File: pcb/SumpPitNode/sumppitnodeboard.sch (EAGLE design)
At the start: 21 parts

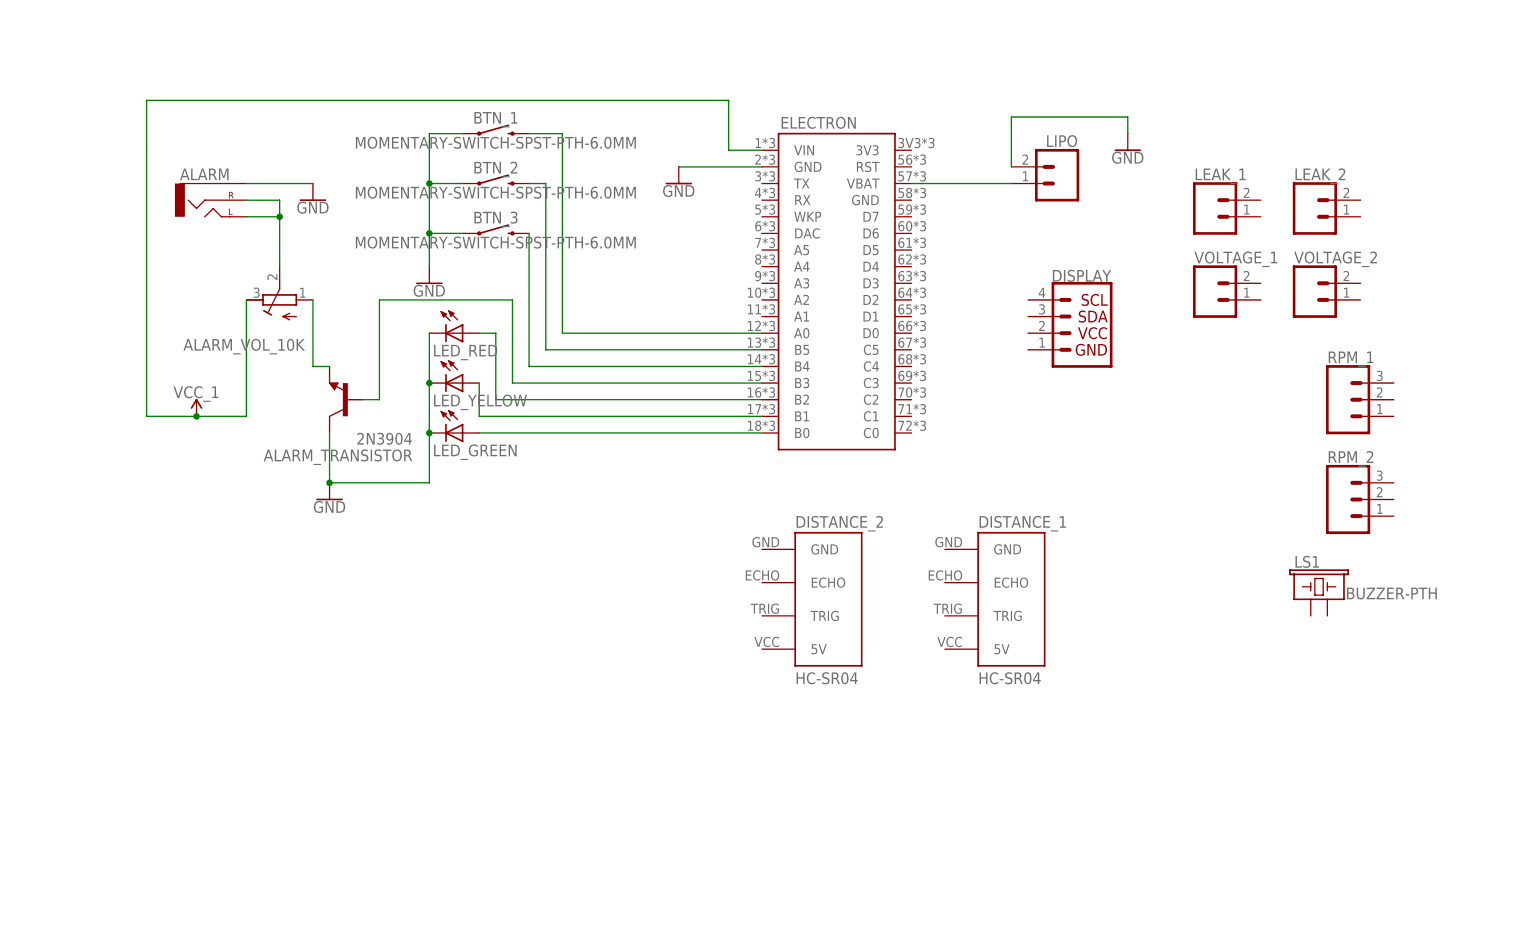
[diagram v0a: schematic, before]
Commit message: Connect more wires. distance to interrupt pins. i2c display 5v voltage regulator for distance sensor. add resistors for leds.
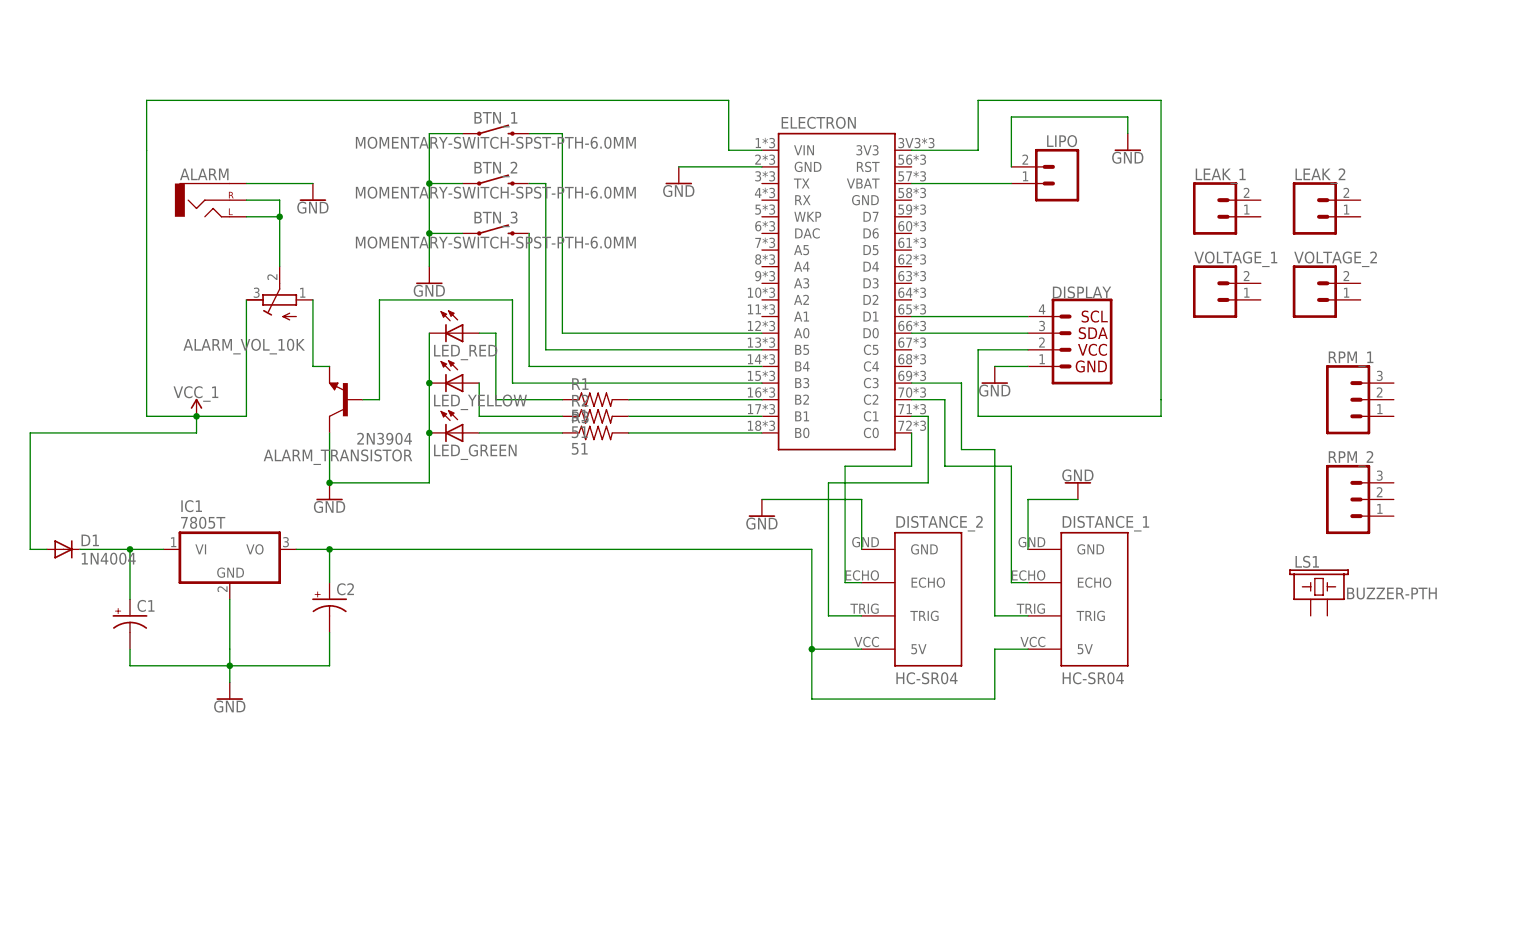
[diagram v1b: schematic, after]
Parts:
- added C1, C2: (no value), rcl:CPOL-USE1.8-4
- added D1: 1N4004, diode:1N4004
- added IC1: 7805T, linear:7805T
- added R1, R2, R3: 51, resistor:R-US_0204/5
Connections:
- new net N$11: DISPLAY.3, ELECTRON.D0
- new net N$12: DISPLAY.4, ELECTRON.D1
- new net N$13: DISTANCE_1.ECHO, ELECTRON.C2
- new net N$14: DISPLAY.2, ELECTRON.3V3
- new net N$15: DISTANCE_2.ECHO, ELECTRON.C0
- new net N$16: DISTANCE_2.TRIG, ELECTRON.C1
- new net N$17: DISTANCE_1.TRIG, ELECTRON.C3
- new net N$18: C1.+, D1.C, IC1.VI
- new net N$19: ELECTRON.B2, R1.2
- new net N$20: LED_YELLOW.A, R2.1
- new net N$21: LED_GREEN.A, R3.1
- new net N$23: C2.+, DISTANCE_1.5V, DISTANCE_2.5V, IC1.VO
- net B$11: now also D1.A
- net GND: now also C1.-, C2.-, DISPLAY.1, DISTANCE_1.GND, DISTANCE_2.GND, IC1.GND
- net N$4: now also R1.1; no longer ELECTRON.B2
- net N$5: now also R2.2; no longer LED_YELLOW.A
- net N$6: now also R3.2; no longer LED_GREEN.A
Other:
- moved on the sheet: DISPLAY, DISTANCE_1, DISTANCE_2

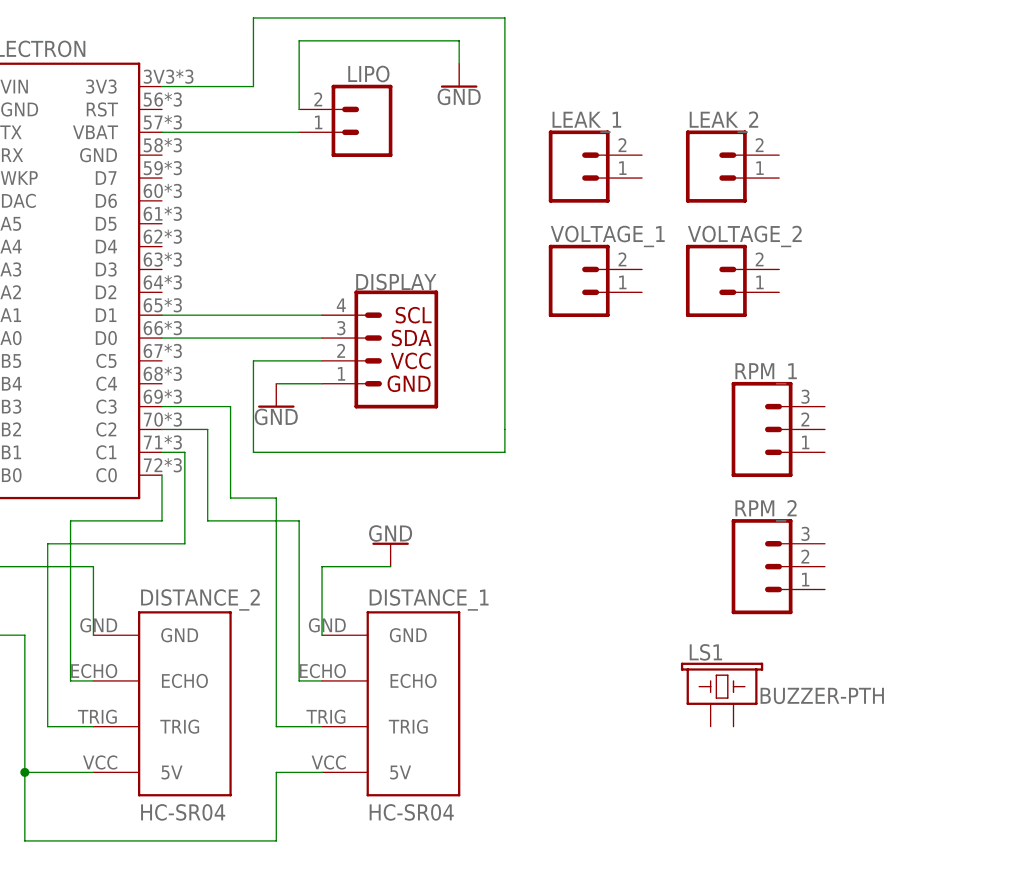
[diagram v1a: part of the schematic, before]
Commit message: Connect buzzer.
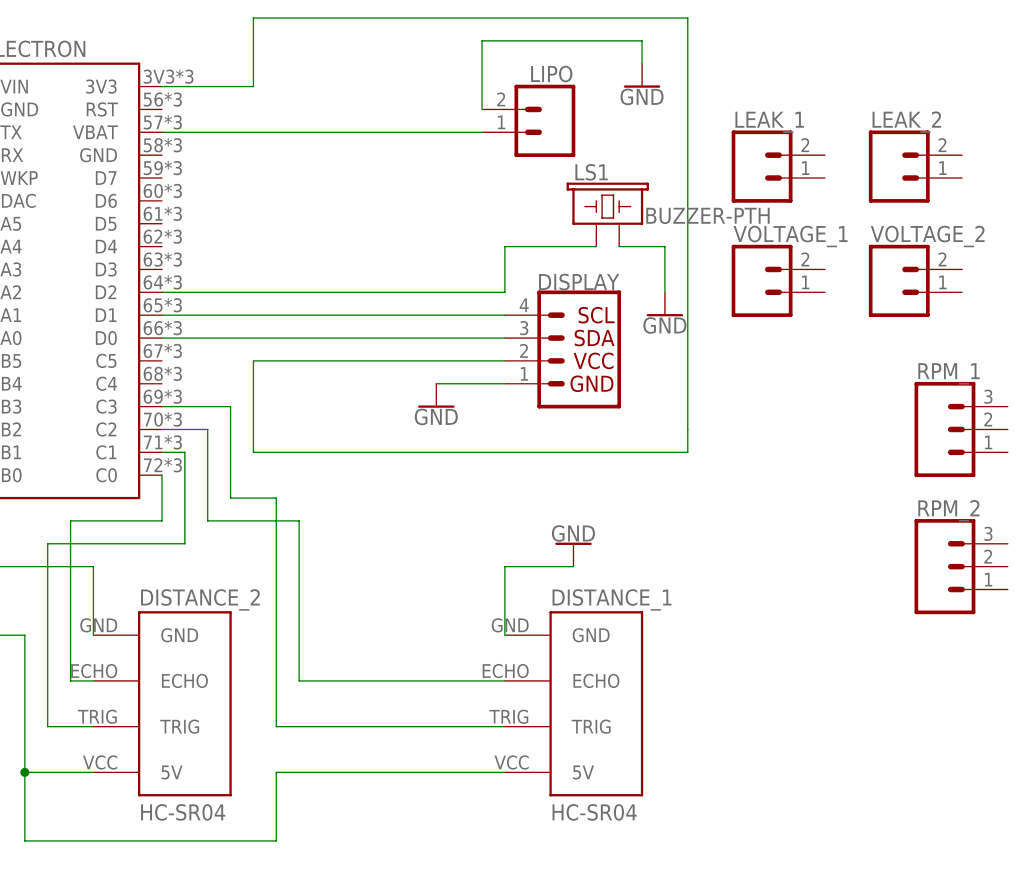
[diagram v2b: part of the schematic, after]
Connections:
- new net N$22: ELECTRON.D2, LS1.1
- net GND: now also LS1.2
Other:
- moved on the sheet: DISPLAY, DISTANCE_1, LEAK_1, LEAK_2, LIPO, LS1, RPM_1, RPM_2, VOLTAGE_1, VOLTAGE_2
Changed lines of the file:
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@@
 <part name="R2" library="resistor" library_urn="urn:adsk.eagle:library:348" deviceset="R-US_" device="0204/5" package3d_urn="urn:adsk.eagle:package:25955/1" value="51"/>
 <part name="R3" library="resistor" library_urn="urn:adsk.eagle:library:348" deviceset="R-US_" device="0204/5" package3d_urn="urn:adsk.eagle:package:25955/1" value="51"/>
+<part name="GND10" library="SparkFun-PowerSymbols" library_urn="urn:adsk.eagle:library:530" deviceset="GND" device=""/>
 </parts>
 <sheets>
@@
 <instances>
 <instance part="ELECTRON" gate="G$1" x="-35.56" y="60.96"/>
-<instance part="DISPLAY" gate="G$1" x="2.54" y="50.8" rot="MR0"/>
-<instance part="DISTANCE_1" gate="J_ULTRASONIC" x="7.62" y="12.7"/>
+<instance part="DISPLAY" gate="G$1" x="22.86" y="50.8" rot="MR0"/>
+<instance part="DISTANCE_1" gate="J_ULTRASONIC" x="27.94" y="12.7"/>
 <instance part="DISTANCE_2" gate="J_ULTRASONIC" x="-17.78" y="12.7"/>
-<instance part="LEAK_1" gate="G$1" x="22.86" y="71.12"/>
-<instance part="LEAK_2" gate="G$1" x="38.1" y="71.12"/>
-<instance part="VOLTAGE_1" gate="G$1" x="22.86" y="58.42"/>
-<instance part="VOLTAGE_2" gate="G$1" x="38.1" y="58.42"/>
-<instance part="RPM_1" gate="J$1" x="43.18" y="43.18"/>
-<instance part="RPM_2" gate="J$1" x="43.18" y="27.94"/>
+<instance part="LEAK_1" gate="G$1" x="43.18" y="71.12"/>
+<instance part="LEAK_2" gate="G$1" x="58.42" y="71.12"/>
+<instance part="VOLTAGE_1" gate="G$1" x="43.18" y="58.42"/>
+<instance part="VOLTAGE_2" gate="G$1" x="58.42" y="58.42"/>
+<instance part="RPM_1" gate="J$1" x="63.5" y="43.18"/>
+<instance part="RPM_2" gate="J$1" x="63.5" y="27.94"/>
 <instance part="LED_YELLOW" gate="G$1" x="-91.44" y="45.72" rot="R270"/>
 <instance part="LED_GREEN" gate="G$1" x="-91.44" y="38.1" rot="R270"/>
 <instance part="LED_RED" gate="G$1" x="-91.44" y="53.34" rot="R270"/>
-<instance part="LS1" gate="G$1" x="38.1" y="12.7"/>
+<instance part="LS1" gate="G$1" x="25.4" y="66.04"/>
 <instance part="ALARM" gate="G$1" x="-129.54" y="73.66"/>
 <instance part="BTN_1" gate="G$1" x="-86.36" y="83.82"/>
 <instance part="BTN_2" gate="G$1" x="-86.36" y="76.2"/>
 <instance part="BTN_3" gate="G$1" x="-86.36" y="68.58"/>
-<instance part="LIPO" gate="G$1" x="0" y="76.2" rot="MR0"/>
+<instance part="LIPO" gate="G$1" x="20.32" y="76.2" rot="MR0"/>
 <instance part="ALARM_TRANSISTOR" gate="G1" x="-109.22" y="43.18" rot="R180"/>
 <instance part="ALARM_VOL_10K" gate="G$1" x="-119.38" y="58.42" rot="R90"/>
@@
 <instance part="GND2" gate="1" x="-111.76" y="27.94"/>
 <instance part="GND3" gate="1" x="-58.42" y="76.2"/>
-<instance part="GND4" gate="1" x="10.16" y="81.28"/>
+<instance part="GND4" gate="1" x="30.48" y="81.28"/>
 <instance part="GND5" gate="1" x="-96.52" y="60.96"/>
-<instance part="GND6" gate="1" x="-10.16" y="45.72"/>
+<instance part="GND6" gate="1" x="7.62" y="45.72"/>
 <instance part="IC1" gate="A1" x="-127" y="20.32"/>
 <instance part="D1" gate="1" x="-152.4" y="20.32"/>
@@
 <instance part="C2" gate="G$1" x="-111.76" y="12.7"/>
 <instance part="GND7" gate="1" x="-127" y="-2.54"/>
-<instance part="GND8" gate="1" x="2.54" y="30.48" rot="R180"/>
+<instance part="GND8" gate="1" x="22.86" y="30.48" rot="R180"/>
 <instance part="GND9" gate="1" x="-45.72" y="25.4"/>
 <instance part="R1" gate="G$1" x="-71.12" y="43.18"/>
 <instance part="R2" gate="G$1" x="-71.12" y="40.64"/>
 <instance part="R3" gate="G$1" x="-71.12" y="38.1"/>
+<instance part="GND10" gate="1" x="33.02" y="55.88"/>
 </instances>
 <busses>
@@
 <segment>
 <pinref part="LIPO" gate="G$1" pin="2"/>
-<wire x1="-7.62" y1="78.74" x2="-7.62" y2="86.36" width="0.1524" layer="91"/>
-<wire x1="-7.62" y1="86.36" x2="10.16" y2="86.36" width="0.1524" layer="91"/>
+<wire x1="12.7" y1="78.74" x2="12.7" y2="86.36" width="0.1524" layer="91"/>
+<wire x1="12.7" y1="86.36" x2="30.48" y2="86.36" width="0.1524" layer="91"/>
 <pinref part="GND4" gate="1" pin="GND"/>
-<wire x1="10.16" y1="86.36" x2="10.16" y2="83.82" width="0.1524" layer="91"/>
+<wire x1="30.48" y1="86.36" x2="30.48" y2="83.82" width="0.1524" layer="91"/>
 </segment>
 <segment>
@@
 <pinref part="GND6" gate="1" pin="GND"/>
 <pinref part="DISPLAY" gate="G$1" pin="1"/>
-<wire x1="-10.16" y1="48.26" x2="-5.08" y2="48.26" width="0.1524" layer="91"/>
+<wire x1="7.62" y1="48.26" x2="15.24" y2="48.26" width="0.1524" layer="91"/>
 </segment>
 <segment>
@@
 <segment>
 <pinref part="DISTANCE_1" gate="J_ULTRASONIC" pin="GND"/>
-<wire x1="-5.08" y1="20.32" x2="-5.08" y2="27.94" width="0.1524" layer="91"/>
+<wire x1="15.24" y1="20.32" x2="15.24" y2="27.94" width="0.1524" layer="91"/>
 <pinref part="GND8" gate="1" pin="GND"/>
-<wire x1="-5.08" y1="27.94" x2="2.54" y2="27.94" width="0.1524" layer="91"/>
+<wire x1="15.24" y1="27.94" x2="22.86" y2="27.94" width="0.1524" layer="91"/>
+</segment>
+<segment>
+<pinref part="LS1" gate="G$1" pin="2"/>
+<wire x1="27.94" y1="63.5" x2="33.02" y2="63.5" width="0.1524" layer="91"/>
+<pinref part="GND10" gate="1" pin="GND"/>
+<wire x1="33.02" y1="63.5" x2="33.02" y2="58.42" width="0.1524" layer="91"/>
 </segment>
 </net>
@@
 <pinref part="LIPO" gate="G$1" pin="1"/>
 <pinref part="ELECTRON" gate="G$1" pin="VBAT"/>
-<wire x1="-7.62" y1="76.2" x2="-22.86" y2="76.2" width="0.1524" layer="91"/>
+<wire x1="12.7" y1="76.2" x2="-22.86" y2="76.2" width="0.1524" layer="91"/>
 </segment>
 </net>
@@
 <pinref part="ELECTRON" gate="G$1" pin="D0"/>
 <pinref part="DISPLAY" gate="G$1" pin="3"/>
-<wire x1="-22.86" y1="53.34" x2="-5.08" y2="53.34" width="0.1524" layer="91"/>
+<wire x1="-22.86" y1="53.34" x2="15.24" y2="53.34" width="0.1524" layer="91"/>
 </segment>
 </net>
@@
 <pinref part="DISPLAY" gate="G$1" pin="4"/>
 <pinref part="ELECTRON" gate="G$1" pin="D1"/>
-<wire x1="-5.08" y1="55.88" x2="-22.86" y2="55.88" width="0.1524" layer="91"/>
+<wire x1="15.24" y1="55.88" x2="-22.86" y2="55.88" width="0.1524" layer="91"/>
 </segment>
 </net>
@@
 <segment>
 <pinref part="DISPLAY" gate="G$1" pin="2"/>
-<wire x1="-12.7" y1="50.8" x2="-5.08" y2="50.8" width="0.1524" layer="91"/>
+<wire x1="-12.7" y1="50.8" x2="15.24" y2="50.8" width="0.1524" layer="91"/>
 <wire x1="-12.7" y1="50.8" x2="-12.7" y2="40.64" width="0.1524" layer="91"/>
-<wire x1="-12.7" y1="40.64" x2="15.24" y2="40.64" width="0.1524" layer="91"/>
-<wire x1="15.24" y1="40.64" x2="15.24" y2="43.18" width="0.1524" layer="91"/>
-<wire x1="15.24" y1="43.18" x2="15.24" y2="88.9" width="0.1524" layer="91"/>
-<wire x1="15.24" y1="88.9" x2="-12.7" y2="88.9" width="0.1524" layer="91"/>
+<wire x1="-12.7" y1="40.64" x2="35.56" y2="40.64" width="0.1524" layer="91"/>
+<wire x1="35.56" y1="40.64" x2="35.56" y2="43.18" width="0.1524" layer="91"/>
+<wire x1="35.56" y1="43.18" x2="35.56" y2="88.9" width="0.1524" layer="91"/>
+<wire x1="35.56" y1="88.9" x2="-12.7" y2="88.9" width="0.1524" layer="91"/>
 <pinref part="ELECTRON" gate="G$1" pin="3V3"/>
 <wire x1="-22.86" y1="81.28" x2="-12.7" y2="81.28" width="0.1524" layer="91"/>
@@
 <segment>
 <pinref part="DISTANCE_1" gate="J_ULTRASONIC" pin="ECHO"/>
-<wire x1="-5.08" y1="15.24" x2="-7.62" y2="15.24" width="0.1524" layer="91"/>
+<wire x1="15.24" y1="15.24" x2="-7.62" y2="15.24" width="0.1524" layer="91"/>
 <wire x1="-7.62" y1="15.24" x2="-7.62" y2="33.02" width="0.1524" layer="91"/>
 <wire x1="-7.62" y1="33.02" x2="-17.78" y2="33.02" width="0.1524" layer="91"/>
@@
 <wire x1="-10.16" y1="35.56" x2="-10.16" y2="10.16" width="0.1524" layer="91"/>
 <pinref part="DISTANCE_1" gate="J_ULTRASONIC" pin="TRIG"/>
-<wire x1="-10.16" y1="10.16" x2="-5.08" y2="10.16" width="0.1524" layer="91"/>
+<wire x1="-10.16" y1="10.16" x2="15.24" y2="10.16" width="0.1524" layer="91"/>
 </segment>
 </net>
@@
 <wire x1="-38.1" y1="5.08" x2="-38.1" y2="20.32" width="0.1524" layer="91"/>
 <pinref part="DISTANCE_1" gate="J_ULTRASONIC" pin="5V"/>
-<wire x1="-5.08" y1="5.08" x2="-10.16" y2="5.08" width="0.1524" layer="91"/>
+<wire x1="15.24" y1="5.08" x2="-10.16" y2="5.08" width="0.1524" layer="91"/>
 <wire x1="-10.16" y1="5.08" x2="-10.16" y2="-2.54" width="0.1524" layer="91"/>
 <wire x1="-10.16" y1="-2.54" x2="-38.1" y2="-2.54" width="0.1524" layer="91"/>
@@
 </segment>
 </net>
+<net name="N$22" class="0">
+<segment>
+<pinref part="LS1" gate="G$1" pin="1"/>
+<wire x1="25.4" y1="63.5" x2="15.24" y2="63.5" width="0.1524" layer="91"/>
+<wire x1="15.24" y1="63.5" x2="15.24" y2="58.42" width="0.1524" layer="91"/>
+<pinref part="ELECTRON" gate="G$1" pin="D2"/>
+<wire x1="15.24" y1="58.42" x2="-22.86" y2="58.42" width="0.1524" layer="91"/>
+</segment>
+</net>
